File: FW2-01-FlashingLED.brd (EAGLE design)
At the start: 125 x 34 mm, 12 parts, among them Q1 BC547, Q3 BC547

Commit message: Basic board layout. Maybe almost done, needs a review
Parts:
- removed JP3: PWR+, freetronics-master-v1.1:1X01
- removed JP4: PWR-, freetronics-master-v1.1:1X01
- removed Q3: BC547, freetronics-master-v1.1:TO-92
- added JP1: PWR+, freetronics-master-v1.1:1X01
- added JP2: PWR-, freetronics-master-v1.1:1X01
- added Q2: BC547, freetronics-master-v1.1:TO-92
- C1: value 2.2uF -> 10uF; device SparkFun:CPOL-RADIAL-100UF-25V -> adafruit:E5-5
- C2: device SparkFun:CPOL-RADIAL-100UF-25V -> adafruit:E5-5
- R1, R4: value 4K7 -> 330R
- R2, R3: value 4K7 -> 47K
- moved R4 54.9 mm to (50.0, 18.0), turned to 90 degrees
- moved C1 46.4 mm to (32.0, 18.0), turned to 270 degrees
- moved R3 37.1 mm to (26.0, 20.0), turned to 90 degrees
- moved R1 30.0 mm to (22.0, 18.0), turned to 90 degrees
- moved Q1 27.8 mm to (29.0, 8.00), turned to 270 degrees
- moved R2 18.1 mm to (46.0, 20.0)
- moved LED1 16.7 mm to (29.0, 29.0)
- moved LED2 10.3 mm to (43.0, 29.0), turned to 180 degrees
- moved C2 9.32 mm to (40.0, 18.0), turned to 270 degrees
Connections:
- new net N$2: JP1.1, LED1.A, LED2.A, R2.P$2, R3.P$2
- new net N$3: C1.+, Q1.1, R1.P$1
- new net N$4: C2.+, Q2.1, R4.P$1
- new net N$5: LED2.K, R4.P$2
- new net N$7: C2.-, Q1.2, R3.P$1
- new net N$8: C1.-, Q2.2, R2.P$1
- new net N$9: JP2.1, Q1.3, Q2.3
- net N$1: now also R1.P$2; no longer R2.P$2
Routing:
- net N$2: track 0.00 -> 27.9 mm
- net N$8: track 0.00 -> 26.8 mm
- net N$4: track 0.00 -> 22.1 mm
- net N$3: track 0.00 -> 20.5 mm
- net N$7: track 0.00 -> 20.2 mm
- net N$9: track 0.00 -> 15.9 mm
- net N$5: track 0.00 -> 12.4 mm
- net N$1: track 0.00 -> 12.4 mm
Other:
- board size 125 x 34 mm -> 71.7 x 37 mm
- board text added: "3-12Vdc"
- board text added: "Flashing LED"
- board text added: "SKU: FW2FLASH"
- board text added: "tron.cc/fw2-flash"
- board text removed: "9Vdc"
- board text removed: "INPUT"
- board text removed: "LED Level Display"
- board text removed: "SKU: FW2LEVEL"
- board text removed: "tron.cc/fw2-level"

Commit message: Updated silkscreen and labels
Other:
- board text added: ""Fun Way Into Electronics""
- board text removed: ""Funway Into Electronics""
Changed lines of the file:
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@@
 <text x="11.918" y="31.35" size="1.27" layer="22" font="vector" ratio="16" rot="SMR270">SKU: FW2FLASH</text>
 <text x="65.868" y="4.048" size="1.2446" layer="21" font="vector" ratio="15" rot="R90">Compatible with Dick Smith's</text>
-<text x="67.9" y="4.048" size="1.2446" layer="21" font="vector" ratio="15" rot="R90">"Funway Into Electronics"</text>
+<text x="67.9" y="4.048" size="1.2446" layer="21" font="vector" ratio="15" rot="R90">"Fun Way Into Electronics"</text>
 <wire x1="38.048" y1="3.34" x2="40.08" y2="3.34" width="0.4064" layer="21"/>
 <wire x1="38.048" y1="34.42" x2="40.08" y2="34.42" width="0.4064" layer="21"/>

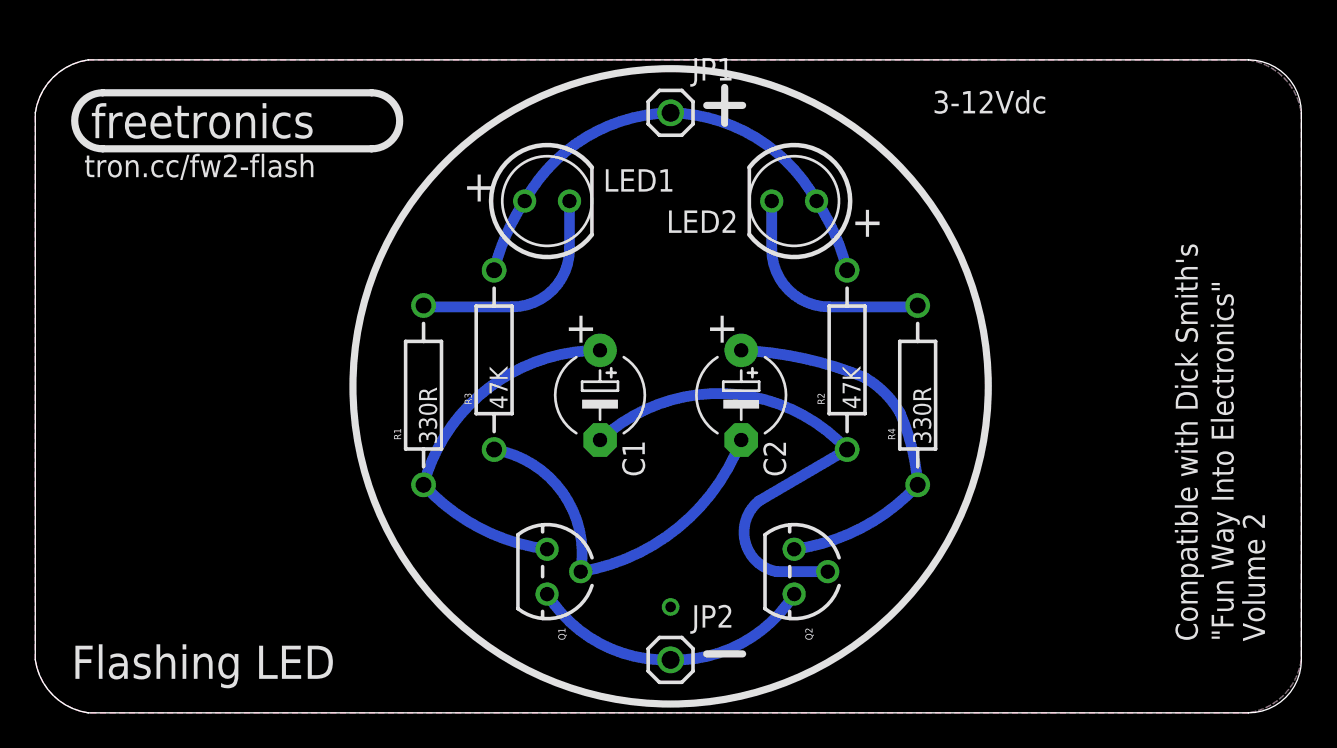
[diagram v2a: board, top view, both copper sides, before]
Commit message: Increased pad size and track width
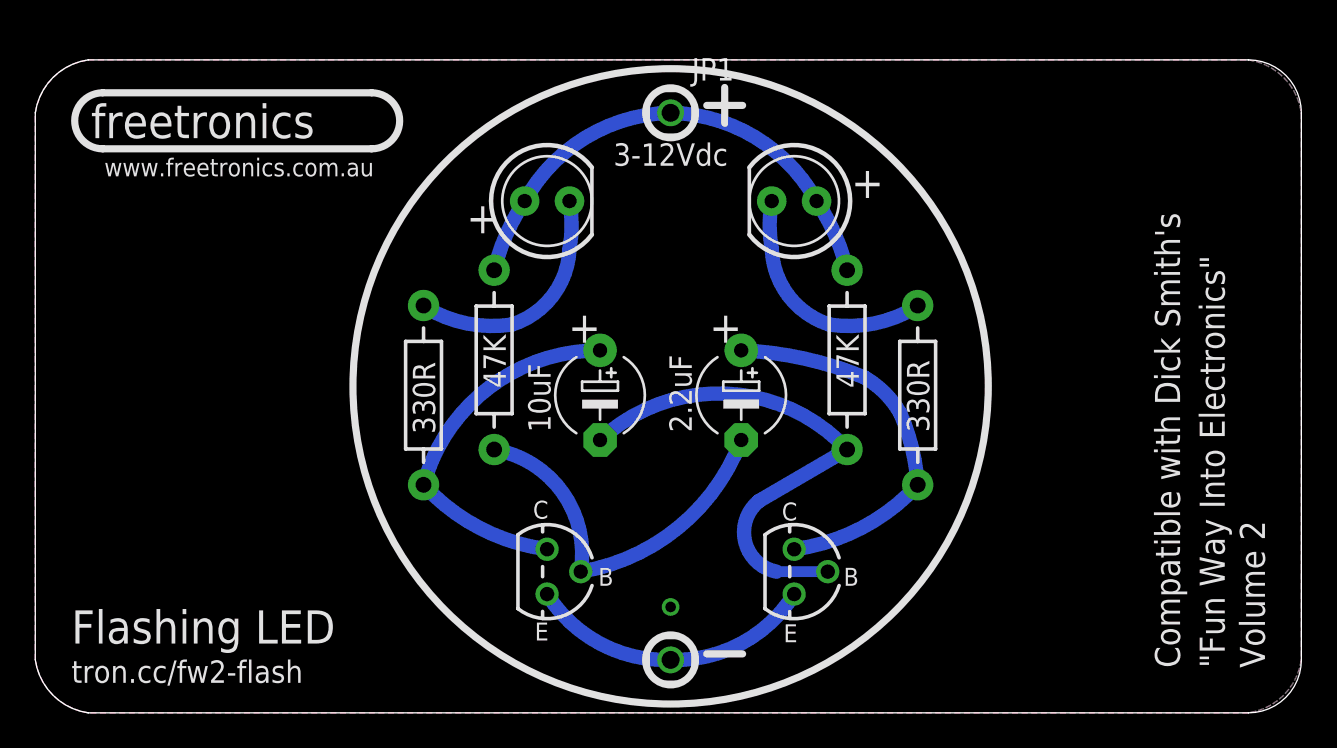
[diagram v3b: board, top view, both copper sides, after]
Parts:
- LED1, LED2: device freetronics-master-v1.1:LED5MM -> freetronics-master-v1.1:LED5MMLARGE
- Q1, Q2: value BC547 -> BC548
- R1, R2, R3, R4: device freetronics:FREETRONICS_AXIAL-0.4 -> freetronics:AXIAL-0.4-LARGE
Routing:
- net N$5: track 12.4 -> 13.2 mm
- net N$1: track 12.4 -> 13.2 mm
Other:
- board text added: "10uF"
- board text added: "2.2uF"
- board text added: "B"
- board text added: "C"
- board text added: "E"
- board text added: "v1.0"
- board text added: "www.freetronics.com.au"
